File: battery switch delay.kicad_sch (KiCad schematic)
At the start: 11 parts, among them J1 5mm pitch 4 position screw te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, K2 G6E-134P-US, Q1 Q_NPN, U2 MIC2920A-12WS-TR_SOT223

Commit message: changed relay to smth with a much lower price .63 vs /bin/zsh.70 🤯
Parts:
- removed K2: G6E-134P-US, Relay_THT:Relay_SPDT_Omron_G6E, symbol Relay:G6E
- added K1: FINDER-36.11, Relay_THT:Relay_SPDT_Finder_36.11, symbol Relay:FINDER-36.11
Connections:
- net +12V: now also K1.A1
- net GND: now also K1.A2
- net ctrl: now also K1.12
- net to switch: now also K1.11
- net at Q1.3 (C), R1.2: now also K1.14
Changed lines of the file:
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@@
-	)
-	(symbol
-		(lib_id "Relay:G6E")
-		(at 45.72 60.96 270)
-		(unit 1)
-		(exclude_from_sim no)
-		(in_bom yes)
-		(on_board yes)
-		(dnp no)
-		(fields_autoplaced yes)
-		(property "Reference" "K2"
-			(at 45.72 45.72 90)
-			(effects
-				(font
-					(size 1.27 1.27)
-				)
-			)
-		)
-		(property "Value" "G6E-134P-US"
-			(at 45.72 48.26 90)
-			(effects
-				(font
-					(size 1.27 1.27)
-				)
-			)
-		)
-		(property "Footprint" "Relay_THT:Relay_SPDT_Omron_G6E"
-			(at 44.958 89.662 0)
-			(effects
-				(font
-					(size 1.27 1.27)
-				)
-				(hide yes)
-			)
-		)
-		(property "Datasheet" "https://www.omron.com/ecb/products/pdf/en-g6e.pdf"
-			(at 45.72 60.96 0)
-			(effects
-				(font
-					(size 1.27 1.27)
-				)
-				(hide yes)
-			)
-		)
-		(property "Description" "Omron Subminiature Sensitive SPDT Signal Switching Relay, Single-Side Stable"
-			(at 45.72 60.96 0)
-			(effects
-				(font
-					(size 1.27 1.27)
-				)
-				(hide yes)
-			)
-		)
-		(pin "12"
-		)
-		(pin "1"
-		)
-		(pin "7"
-		)
-		(pin "6"
-		)
-		(pin "10"
-		)
-		(instances
-			(project ""
-				(path "/72486ea4-2971-4ca2-ab8b-187d20cf76b7"
-					(reference "K2")
-					(unit 1)
-				)
-			)
-		)
 	)
 	(symbol
@@
 					(unit 1)
 				)
+			)
+		)
+	)
+	(symbol
+		(lib_id "Relay:FINDER-36.11")
+		(at 45.72 60.96 270)
+		(unit 1)
+		(exclude_from_sim no)
+		(in_bom yes)
+		(on_board yes)
+		(dnp no)
+		(fields_autoplaced yes)
+		(property "Reference" "K1"
+			(at 45.72 45.72 90)
+			(effects
+				(font
+					(size 1.27 1.27)
+				)
+			)
+		)
+		(property "Value" "FINDER-36.11"
+			(at 45.72 48.26 90)
+			(effects
+				(font
+					(size 1.27 1.27)
+				)
+			)
+		)
+		(property "Footprint" "Relay_THT:Relay_SPDT_Finder_36.11"
+			(at 44.958 93.218 0)
+			(effects
+				(font
+					(size 1.27 1.27)
+				)
+				(hide yes)
+			)
+		)
+		(property "Datasheet" "https://gfinder.findernet.com/public/attachments/36/EN/S36EN.pdf"
+			(at 45.72 60.96 0)
+			(effects
+				(font
+					(size 1.27 1.27)
+				)
+				(hide yes)
+			)
+		)
+		(property "Description" "FINDER 36.11, SPDT relay, 10A"
+			(at 45.72 60.96 0)
+			(effects
+				(font
+					(size 1.27 1.27)
+				)
+				(hide yes)
+			)
+		)
+		(pin "A2"
+		)
+		(pin "12"
+		)
+		(pin "A1"
+		)
+		(pin "11"
+		)
+		(pin "14"
+		)
+		(instances
+			(project ""
+				(path "/72486ea4-2971-4ca2-ab8b-187d20cf76b7"
+					(reference "K1")
+					(unit 1)
+				)

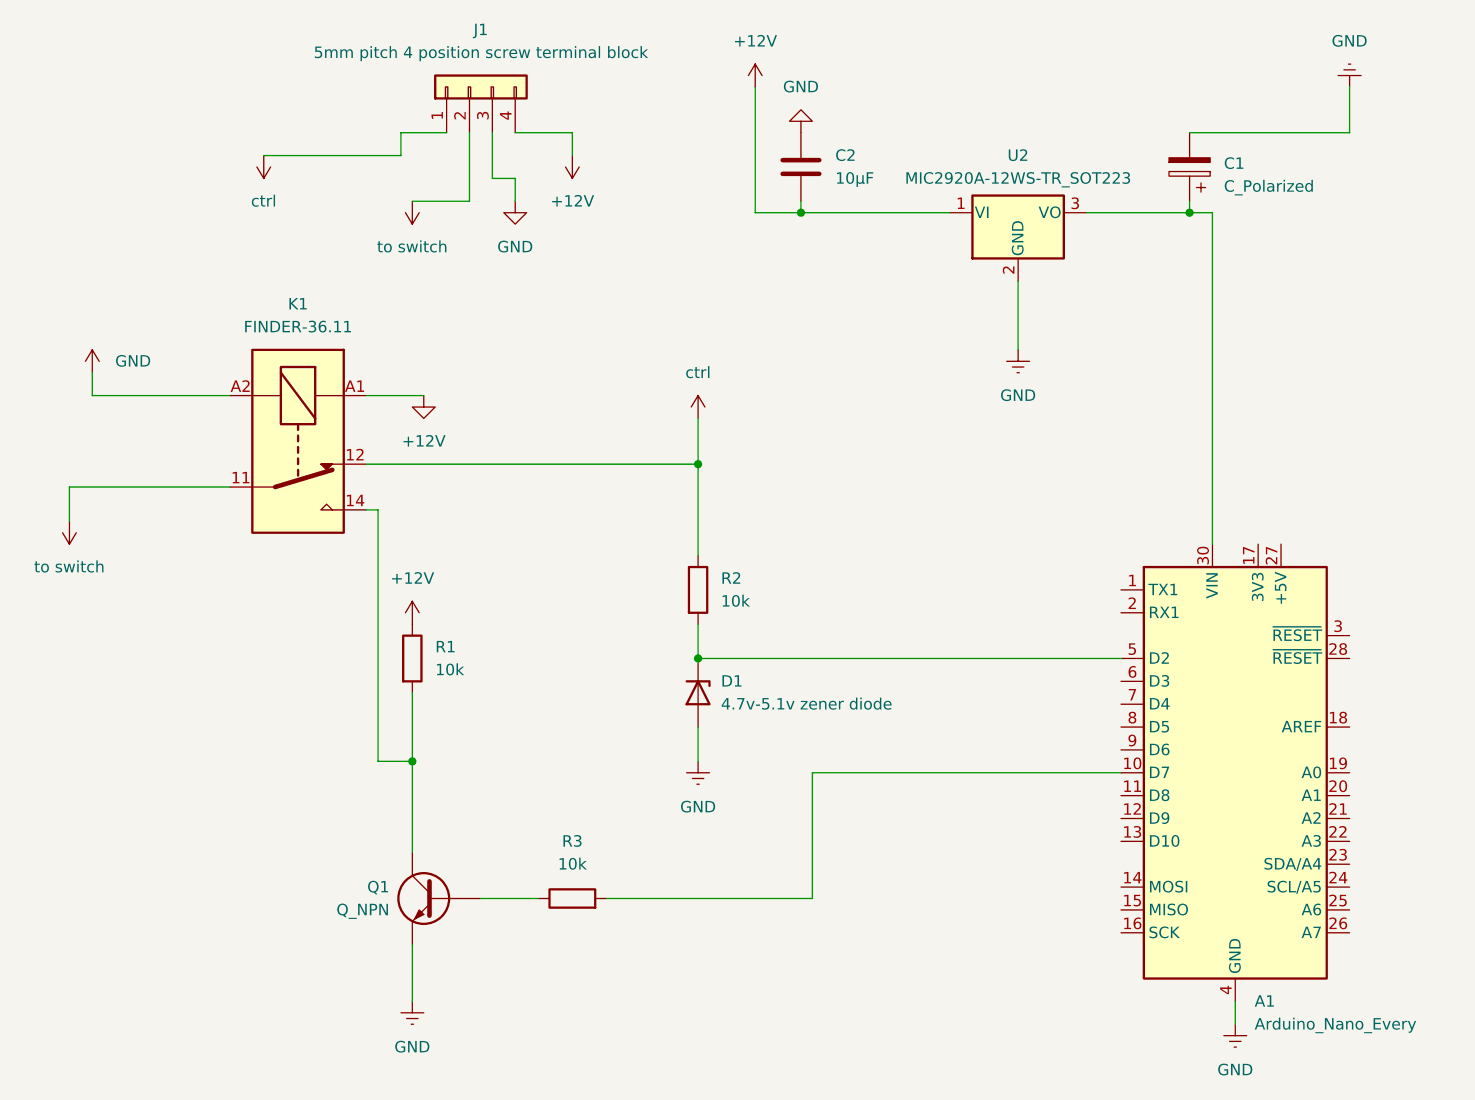
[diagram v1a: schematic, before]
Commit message: added qr code and text to the repo
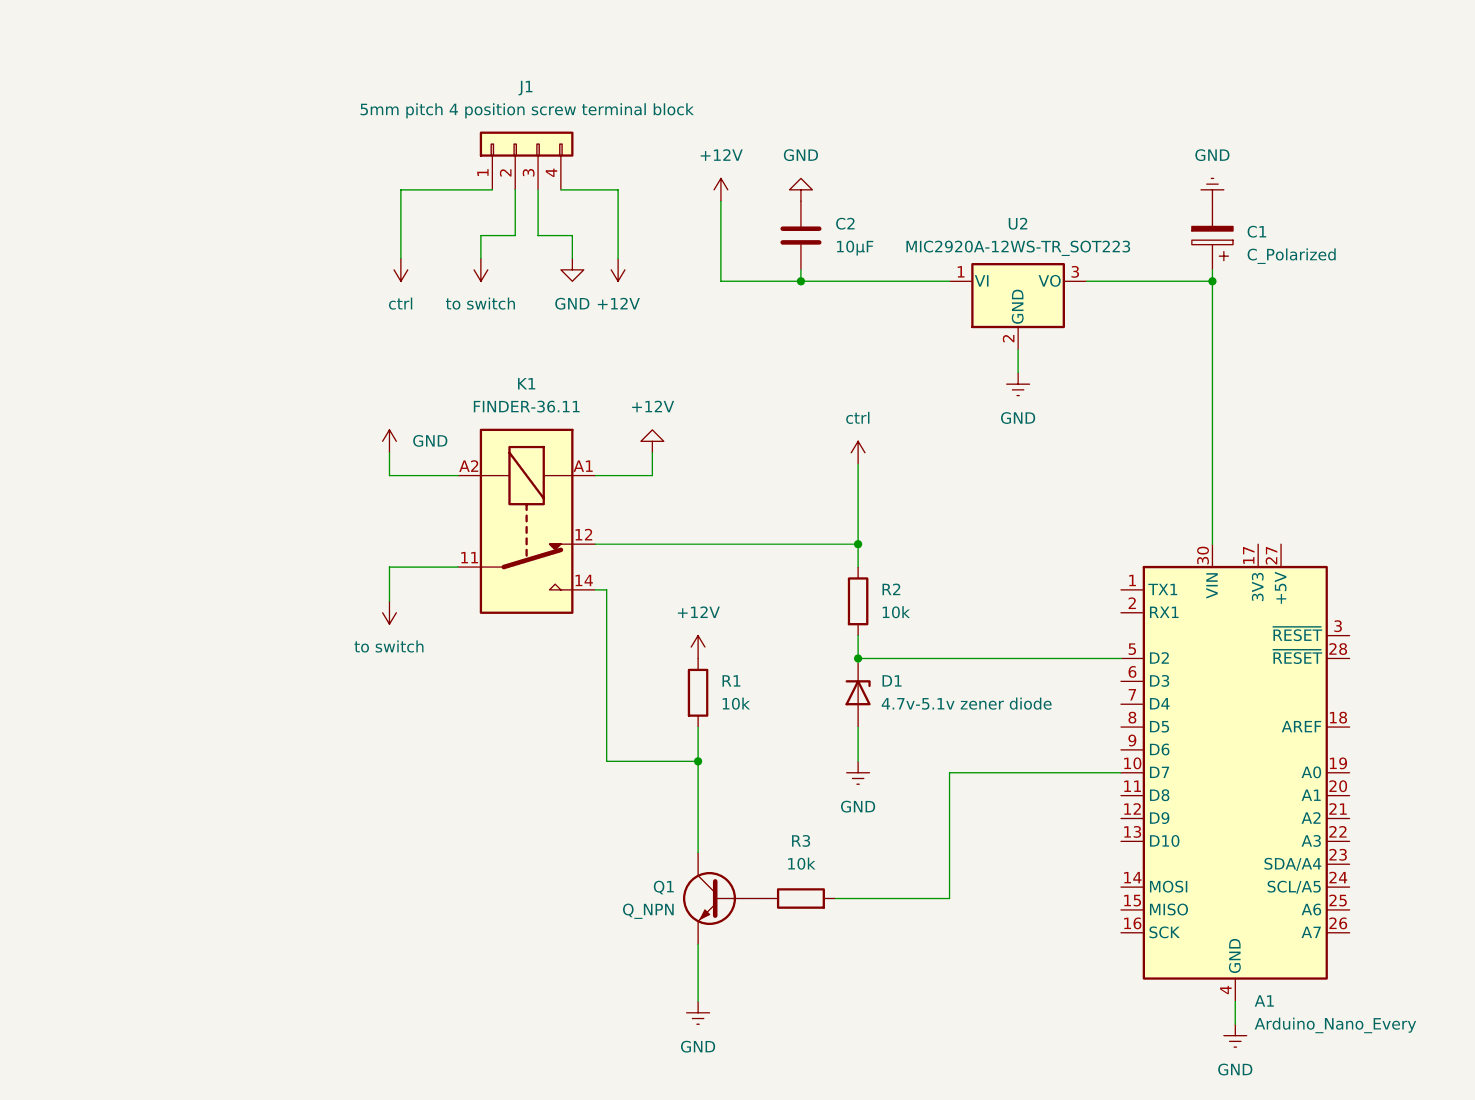
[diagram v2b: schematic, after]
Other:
- moved on the sheet: C1, C2, D1, J1, K1, Q1, R1, R2, R3, U2
